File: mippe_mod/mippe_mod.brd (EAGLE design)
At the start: 32.5 x 50 mm, 24 parts, among them J1 VCC, J12 BURNIN, J2 GND, J3 UART, J4 FTDI, J5 VCC, J6 GND, SW1 BTN-PTS810, U1 LM340MPX-5.0230, U2 ATMEGA328P-AUR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

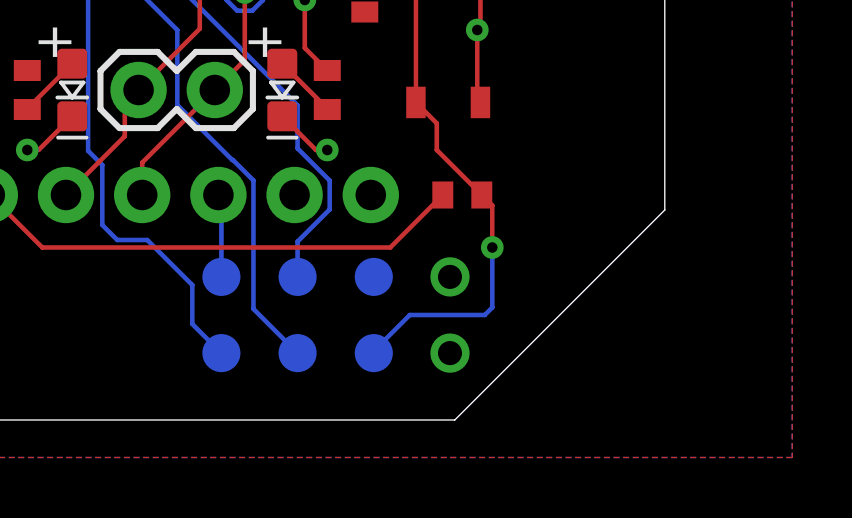
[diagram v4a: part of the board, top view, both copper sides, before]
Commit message: update burnin drill size
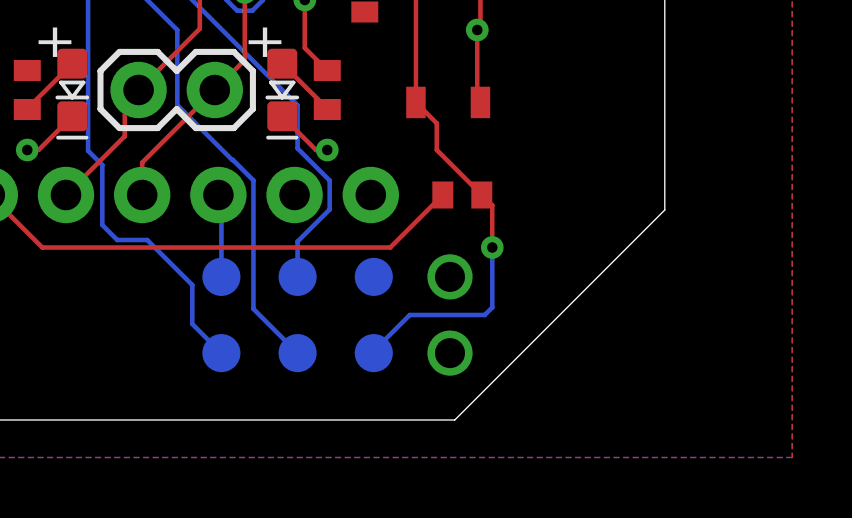
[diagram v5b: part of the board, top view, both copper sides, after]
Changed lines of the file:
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@@
 </groups>
 <elements>
-<element name="C1" library="scono" library_urn="urn:adsk.eagle:library:14850048" package="0402-CAP" package3d_urn="urn:adsk.eagle:package:14850678/2" value="100nF" x="8.25" y="19" smashed="yes">
+<element name="C1" library="scono" library_urn="urn:adsk.eagle:library:14850048" package="0402-CAP" package3d_urn="urn:adsk.eagle:package:14850678/3" value="100nF" x="8.25" y="19" smashed="yes">
 <attribute name="PIE-INT-REF-NUM" value="CAPACITOR-GENERIC" x="46.35" y="-21.64" size="1.778" layer="27" display="off"/>
 <attribute name="VALUE" x="6.98" y="17.73" size="0.508" layer="27" font="vector"/>
 </element>
-<element name="C2" library="scono" library_urn="urn:adsk.eagle:library:14850048" package="0402-CAP" package3d_urn="urn:adsk.eagle:package:14850678/2" value="100nF" x="5.25" y="19" smashed="yes" rot="R180">
+<element name="C2" library="scono" library_urn="urn:adsk.eagle:library:14850048" package="0402-CAP" package3d_urn="urn:adsk.eagle:package:14850678/3" value="100nF" x="5.25" y="19" smashed="yes" rot="R180">
 <attribute name="PIE-INT-REF-NUM" value="CAPACITOR-GENERIC" x="-36.66" y="59.64" size="1.778" layer="27" rot="R180" display="off"/>
 <attribute name="VALUE" x="6.52" y="20.27" size="0.508" layer="27" font="vector" rot="R180"/>
 </element>
-<element name="C3" library="scono" library_urn="urn:adsk.eagle:library:14850048" package="0402-CAP" package3d_urn="urn:adsk.eagle:package:14850678/2" value="100nF" x="10" y="22.25" smashed="yes" rot="R90">
+<element name="C3" library="scono" library_urn="urn:adsk.eagle:library:14850048" package="0402-CAP" package3d_urn="urn:adsk.eagle:package:14850678/3" value="100nF" x="10" y="22.25" smashed="yes" rot="R90">
 <attribute name="PIE-INT-REF-NUM" value="CAPACITOR-GENERIC" x="41.75" y="65.43" size="1.778" layer="27" rot="R90" display="off"/>
 <attribute name="VALUE" x="11.397" y="20.98" size="0.508" layer="27" font="vector" rot="R90"/>
 </element>
-<element name="C4" library="scono" library_urn="urn:adsk.eagle:library:14850048" package="0402-CAP" package3d_urn="urn:adsk.eagle:package:14850678/2" value="100nF" x="22.5" y="22.25" smashed="yes" rot="R90">
+<element name="C4" library="scono" library_urn="urn:adsk.eagle:library:14850048" package="0402-CAP" package3d_urn="urn:adsk.eagle:package:14850678/3" value="100nF" x="22.5" y="22.25" smashed="yes" rot="R90">
 <attribute name="PIE-INT-REF-NUM" value="CAPACITOR-GENERIC" x="59.33" y="37.49" size="1.778" layer="27" rot="R90" display="off"/>
 </element>
-<element name="C5" library="scono" library_urn="urn:adsk.eagle:library:14850048" package="0402-CAP" package3d_urn="urn:adsk.eagle:package:14850678/2" value="18pF" x="26" y="17.75" smashed="yes" grouprefs="XTAL">
+<element name="C5" library="scono" library_urn="urn:adsk.eagle:library:14850048" package="0402-CAP" package3d_urn="urn:adsk.eagle:package:14850678/3" value="18pF" x="26" y="17.75" smashed="yes" grouprefs="XTAL">
 <attribute name="PIE-INT-REF-NUM" value="CAPACITOR-GENERIC" x="46.32" y="-19.08" size="1.778" layer="27" display="off"/>
 </element>
-<element name="C6" library="scono" library_urn="urn:adsk.eagle:library:14850048" package="0402-CAP" package3d_urn="urn:adsk.eagle:package:14850678/2" value="18pF" x="26" y="26.25" smashed="yes" grouprefs="XTAL">
+<element name="C6" library="scono" library_urn="urn:adsk.eagle:library:14850048" package="0402-CAP" package3d_urn="urn:adsk.eagle:package:14850678/3" value="18pF" x="26" y="26.25" smashed="yes" grouprefs="XTAL">
 <attribute name="PIE-INT-REF-NUM" value="CAPACITOR-GENERIC" x="51.4" y="-10.58" size="1.778" layer="27" display="off"/>
 </element>
-<element name="C7" library="scono" library_urn="urn:adsk.eagle:library:14850048" package="0402-CAP" package3d_urn="urn:adsk.eagle:package:14850678/2" value="100nF" x="25.75" y="7.5" smashed="yes" rot="R180">
+<element name="C7" library="scono" library_urn="urn:adsk.eagle:library:14850048" package="0402-CAP" package3d_urn="urn:adsk.eagle:package:14850678/3" value="100nF" x="25.75" y="7.5" smashed="yes" rot="R180">
 <attribute name="PIE-INT-REF-NUM" value="CAPACITOR-GENERIC" x="-4.73" y="44.33" size="1.778" layer="27" rot="R180" display="off"/>
 <attribute name="VALUE" x="27.02" y="8.897" size="0.508" layer="27" font="vector" rot="R180"/>
 </element>
-<element name="D1" library="scono" library_urn="urn:adsk.eagle:library:14850048" package="LED-0603" package3d_urn="urn:adsk.eagle:package:14850721/2" value="" x="19.75" y="11" smashed="yes" rot="R90">
+<element name="D1" library="scono" library_urn="urn:adsk.eagle:library:14850048" package="LED-0603" package3d_urn="urn:adsk.eagle:package:14850721/3" value="" x="19.75" y="11" smashed="yes" rot="R90">
 <attribute name="VALUE" x="20.85" y="9.9" size="0.508" layer="27" font="vector" rot="R90"/>
 </element>
-<element name="D2" library="scono" library_urn="urn:adsk.eagle:library:14850048" package="LED-0603" package3d_urn="urn:adsk.eagle:package:14850721/2" value="RED" x="12.75" y="11" smashed="yes" rot="R90">
+<element name="D2" library="scono" library_urn="urn:adsk.eagle:library:14850048" package="LED-0603" package3d_urn="urn:adsk.eagle:package:14850721/3" value="RED" x="12.75" y="11" smashed="yes" rot="R90">
 <attribute name="VALUE" x="13.85" y="9.9" size="0.508" layer="27" font="vector" rot="R90"/>
 </element>
@@
 <attribute name="VALUE" x="8.73" y="5.468" size="0.6096" layer="27" font="vector" ratio="20"/>
 </element>
-<element name="R1" library="scono" library_urn="urn:adsk.eagle:library:14850048" package="R0402" package3d_urn="urn:adsk.eagle:package:14850590/2" value="10k" x="22.5" y="14.25" smashed="yes" rot="R270">
+<element name="R1" library="scono" library_urn="urn:adsk.eagle:library:14850048" package="R0402" package3d_urn="urn:adsk.eagle:package:14850590/3" value="10k" x="22.5" y="14.25" smashed="yes" rot="R270">
 <attribute name="VALUE" x="21.484" y="15.52" size="0.508" layer="27" font="vector" rot="R270" align="top-left"/>
 </element>
-<element name="R2" library="scono" library_urn="urn:adsk.eagle:library:14850048" package="R0402" package3d_urn="urn:adsk.eagle:package:14850590/2" value="500R" x="21.25" y="11" smashed="yes" rot="R90">
+<element name="R2" library="scono" library_urn="urn:adsk.eagle:library:14850048" package="R0402" package3d_urn="urn:adsk.eagle:package:14850590/3" value="500R" x="21.25" y="11" smashed="yes" rot="R90">
 <attribute name="VALUE" x="22.266" y="9.73" size="0.508" layer="27" font="vector" rot="R90" align="top-left"/>
 </element>
-<element name="R3" library="scono" library_urn="urn:adsk.eagle:library:14850048" package="R0402" package3d_urn="urn:adsk.eagle:package:14850590/2" value="500R" x="11.25" y="11" smashed="yes" rot="R270">
+<element name="R3" library="scono" library_urn="urn:adsk.eagle:library:14850048" package="R0402" package3d_urn="urn:adsk.eagle:package:14850590/3" value="500R" x="11.25" y="11" smashed="yes" rot="R270">
 <attribute name="VALUE" x="10.234" y="12.27" size="0.508" layer="27" font="vector" rot="R270" align="top-left"/>
 </element>
